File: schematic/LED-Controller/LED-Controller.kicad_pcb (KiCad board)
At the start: 2 copper layers, 40.5 x 36.5 mm, 16 parts, among them J1 5V Power, J10 String6, J2 ICSP, J3 RCin, J4 Serial Connect, J5 String1, J6 String2, J7 String3, J8 String4, J9 String5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

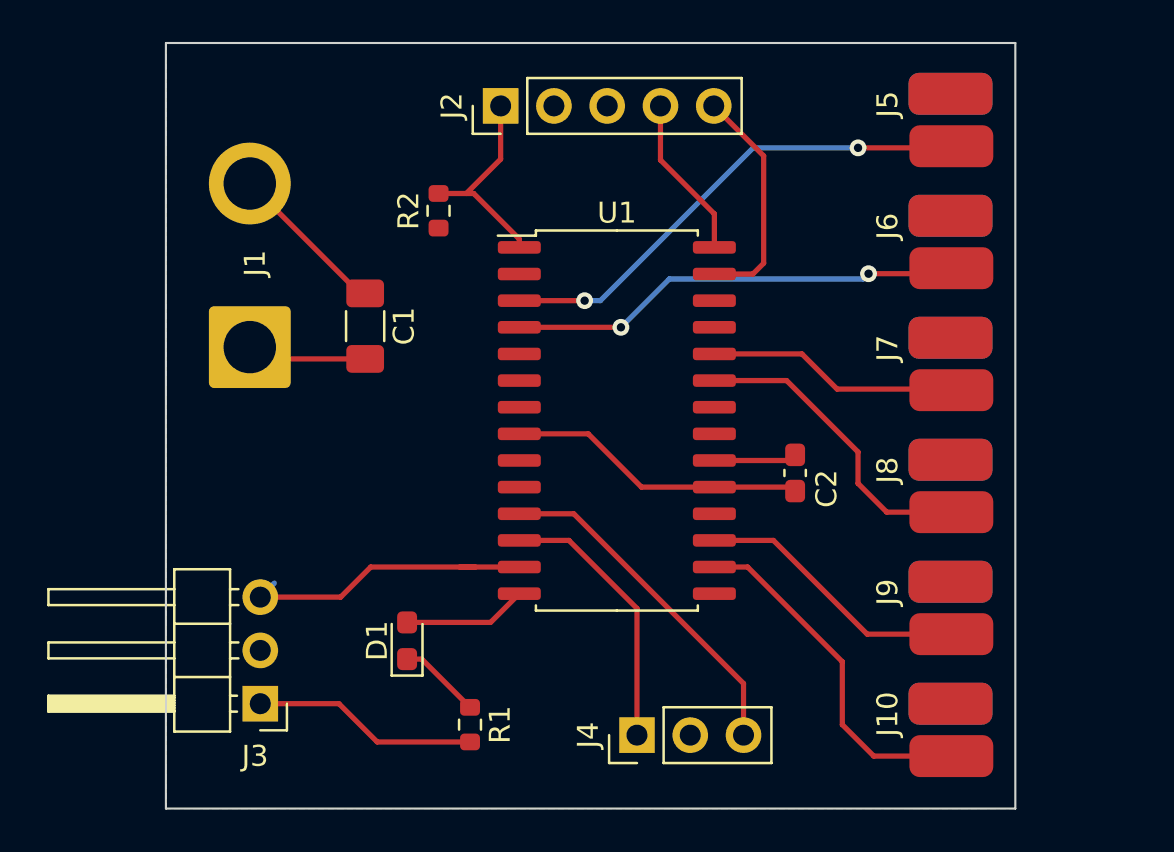
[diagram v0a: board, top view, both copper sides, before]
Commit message: Changed connectors
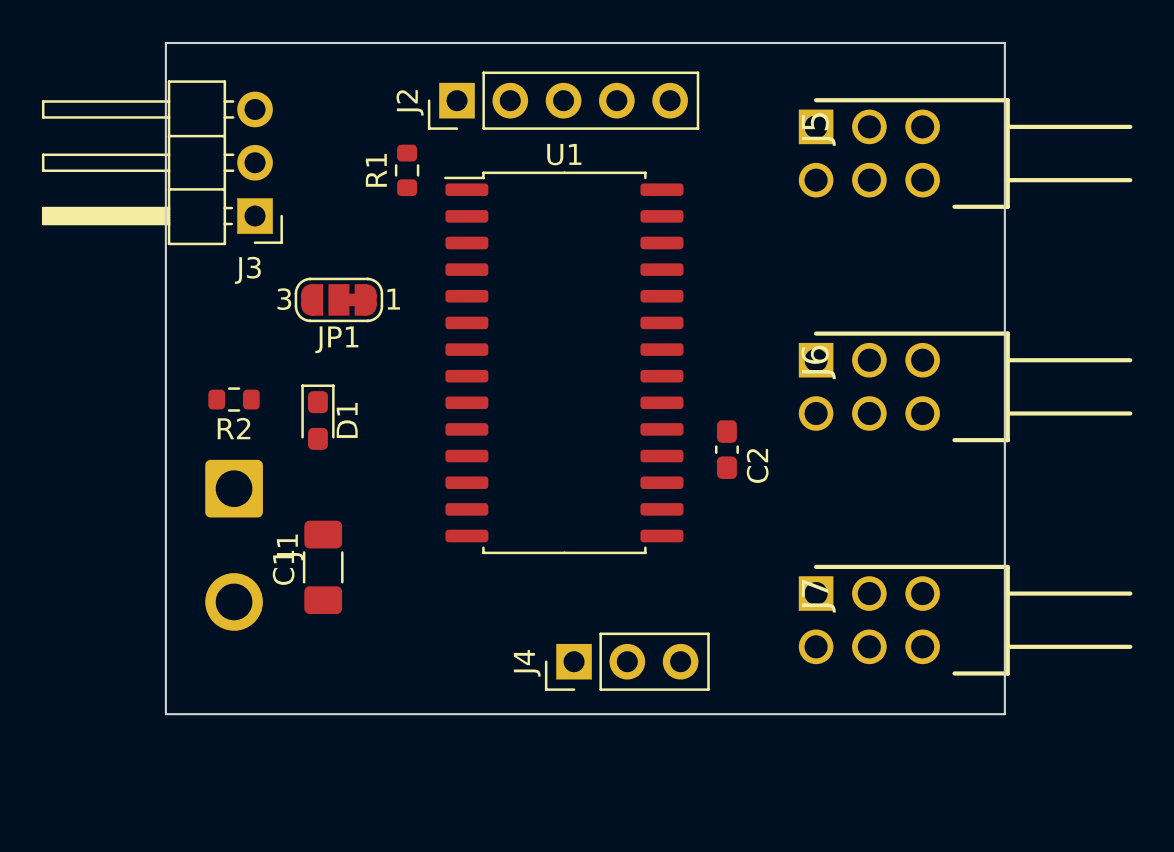
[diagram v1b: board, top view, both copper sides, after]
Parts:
- removed J10: String6, LEDStringConn:TopBottom_3Pin
- removed J8: String4, LEDStringConn:TopBottom_3Pin
- removed J9: String5, LEDStringConn:TopBottom_3Pin
- removed the R1 at (132.5, 102.0)
- added JP1: uC Power, Jumper:SolderJumper-3_P1.3mm_Bridged12_RoundedPad1.0x1.5mm_NumberLabels, F.Cu at (126.2, 81.8)
- added R2: 220, Resistor_SMD:R_0603_1608Metric, F.Cu at (121.2, 86.5)
- J1: footprint Connector_Wire:SolderWire-2sqmm_1x02_P7.8mm_D2mm_OD3.9mm -> Connector_Wire:SolderWire-1sqmm_1x02_P5.4mm_D1.4mm_OD2.7mm
- J5: value String1 -> TSW-102-08-L-T-RA; footprint LEDStringConn:TopBottom_3Pin -> SamacSys_Parts:HDRRA6W64P254_3X2_508X254X810P
- J6: value String2 -> TSW-102-08-L-T-RA; footprint LEDStringConn:TopBottom_3Pin -> SamacSys_Parts:HDRRA6W64P254_3X2_508X254X810P
- J7: value String3 -> TSW-102-08-L-T-RA; footprint LEDStringConn:TopBottom_3Pin -> SamacSys_Parts:HDRRA6W64P254_3X2_508X254X810P
- moved J3 23.3 mm to (122.2, 77.8)
- moved C1 11.7 mm to (125.5, 94.5), turned to 90 degrees
- moved D1 11.3 mm to (125.2, 87.5), turned to 270 degrees
- moved J7 10.5 mm to (149.0, 95.8), turned to 270 degrees
- moved J1 6.79 mm to (121.2, 90.8), turned to 270 degrees
- moved J6 5.88 mm to (149.0, 84.6), turned to 270 degrees
- moved J4 4.61 mm to (137.5, 99.0)
- moved J5 4.02 mm to (149.0, 73.5), turned to 270 degrees
- moved U1 3.72 mm to (137.0, 84.8)
- moved C2 3.44 mm to (144.8, 88.9)
- moved R1 2.44 mm to (129.5, 75.6)
- moved J2 2.09 mm to (131.9, 72.2)
- renumbered R2 to R1
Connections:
- C2 pad 2: VDD -> /uC_Power
- J2 pad 2: VDD -> /uC_Power
- J5 pad 1: VDD -> Net-(J5-Pad1)
- J5 pad 2: Net-(J5-Pad2) -> VDD
- J6 pad 1: VDD -> Net-(J6-Pad1)
- J6 pad 2: Net-(J6-Pad2) -> VDD
- J7 pad 1: VDD -> Net-(J7-Pad1)
- J7 pad 2: Net-(J7-Pad2) -> VDD
- R1 pad 1: VDD -> /uC_Power
- U1 pad 16: Net-(J10-Pad2) -> Net-(J7-Pad4)
- U1 pad 17: Net-(J9-Pad2) -> Net-(J7-Pad1)
- U1 pad 20: VDD -> /uC_Power
- U1 pad 23: Net-(J8-Pad2) -> Net-(J6-Pad4)
- U1 pad 24: Net-(J7-Pad2) -> Net-(J6-Pad1)
- U1 pad 3: Net-(J5-Pad2) -> Net-(J5-Pad1)
- U1 pad 4: Net-(J6-Pad2) -> Net-(J5-Pad4)
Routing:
- net GND: track 31.0 -> 0.00 mm
- net Net-(J5-Pad2): track 23.6 -> 0.00 mm, vias 2 -> 0
- net Net-(J6-Pad2): track 21.8 -> 0.00 mm, vias 2 -> 0
- net Net-(J10-Pad2): track 16.8 -> 0.00 mm
- net Net-(J4-Pad3): track 16.5 -> 0.00 mm
- net Net-(J8-Pad2): track 14.8 -> 0.00 mm
- net Net-(J3-Pad3): track 14.6 -> 0.00 mm
- net Net-(J9-Pad2): track 13.1 -> 0.00 mm
- net Net-(J4-Pad1): track 13.0 -> 0.00 mm
- net Net-(J7-Pad2): track 12.0 -> 0.00 mm
- net VDD: track 11.6 -> 0.00 mm
- net Net-(J2-Pad5): track 11.0 -> 0.00 mm
- net Net-(J2-Pad1): track 10.00 -> 0.00 mm
- net Net-(J2-Pad4): track 7.81 -> 0.00 mm
- net Net-(D1-Pad2): track 5.92 -> 0.00 mm
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- removed copper zone on B.Cu, net GND
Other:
- board size 40.5 x 36.5 mm -> 40 x 32 mm

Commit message: Complete pcb layout
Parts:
- J5, J6, J7: value TSW-102-08-L-T-RA -> (none)
- moved J1 25.5 mm to (146.0, 97.0), turned to 0 degrees
- moved C1 11.7 mm to (137.0, 96.5), turned to 270 degrees
- moved J4 9.54 mm to (128.2, 96.5), turned to 270 degrees
- moved J7 6.75 mm to (148.8, 89.0)
- moved J6 3.38 mm to (148.8, 81.2)
- moved R2 3.09 mm to (122.0, 89.5)
- moved C2 2.65 mm to (145.0, 86.2)
- moved D1 2.46 mm to (126.2, 89.8)
- moved JP1 2.02 mm to (125.2, 83.5)
- moved U1 0.75 mm to (137.0, 84.0)
- moved J2 0.63 mm to (131.5, 71.8)
- moved J5 0.25 mm to (148.8, 73.5)
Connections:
- U1 pad 11: Net-(J4-Pad3) -> Net-(J3-Pad3)
- U1 pad 12: Net-(J4-Pad1) -> Net-(D1-Pad2)
- U1 pad 13: Net-(J3-Pad3) -> Net-(J4-Pad3)
- U1 pad 14: Net-(D1-Pad2) -> Net-(J4-Pad1)
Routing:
- net VDD: track 0.00 -> 81.6 mm, vias 0 -> 2
- net GND: track 0.00 -> 63.5 mm, vias 0 -> 2
- net /uC_Power: track 0.00 -> 38.1 mm, vias 0 -> 3
- net Net-(J3-Pad3): track 0.00 -> 20.3 mm
- net Net-(J5-Pad1): track 0.00 -> 18.4 mm, vias 0 -> 1
- net Net-(J5-Pad4): track 0.00 -> 17.9 mm, vias 0 -> 1
- net Net-(J4-Pad3): track 0.00 -> 12.4 mm
- net Net-(J3-Pad2): track 0.00 -> 9.87 mm
- net Net-(J2-Pad5): track 0.00 -> 9.20 mm
- net Net-(J6-Pad4): track 0.00 -> 7.80 mm
- net Net-(J7-Pad1): track 0.00 -> 7.40 mm
- net Net-(J7-Pad4): track 0.00 -> 7.33 mm
- net Net-(J6-Pad1): track 0.00 -> 7.28 mm
- net Net-(J2-Pad1): track 0.00 -> 7.09 mm
- net Net-(J4-Pad1): track 0.00 -> 7.03 mm
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- added copper zone on B.Cu, net GND
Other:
- board text added: "+"
- board text added: "-"
- board text added: "JLCJLCJLCJLC"
- board text added: "LED Controller"
- board text added: "QES 2021"
- board text added: "V 1.0"

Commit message: Completed pcb
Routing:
- net GND: track 63.5 -> 57.9 mm, vias 2 -> 3
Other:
- rule solder_mask_min_width: 0.25 -> 0.2
- board text added: "1"
- board text added: "2"
- board text added: "3"
- board text added: "4"
- board text added: "5"
- board text added: "6"
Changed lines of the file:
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@@
   (general
     (thickness 1.6)
-    (drawings 42)
-    (tracks 106)
+    (drawings 48)
+    (tracks 108)
     (zones 0)
     (modules 14)
@@
   (page A4)
   (layers
-    (0 F.Cu signal hide)
-    (31 B.Cu signal hide)
+    (0 F.Cu signal)
+    (31 B.Cu signal)
     (32 B.Adhes user hide)
     (33 F.Adhes user hide)
@@
     (36 B.SilkS user)
     (37 F.SilkS user)
-    (38 B.Mask user)
-    (39 F.Mask user)
+    (38 B.Mask user hide)
+    (39 F.Mask user hide)
     (40 Dwgs.User user hide)
     (41 Cmts.User user hide)
@@
     (pad_drill 2.5)
     (pad_to_mask_clearance 0.051)
-    (solder_mask_min_width 0.25)
+    (solder_mask_min_width 0.2)
     (aux_axis_origin 0 0)
     (visible_elements 7FFFFFFF)
@@
     (tags "capacitor handsolder")
     (attr smd)
-    (fp_text reference C2 (at -0.75 1.5 90) (layer F.SilkS)
+    (fp_text reference C2 (at 2.25 -0.5 180) (layer F.SilkS)
       (effects (font (size 1 1) (thickness 0.15)))
     )
@@
       (effects (font (size 0.8 0.8) (thickness 0.12)))
     )
-    (pad 2 smd roundrect (at 1.5625 0 270) (size 1.325 1.8) (layers F.Cu F.Paste F.Mask) (roundrect_rratio 0.1886777358490566)
-      (net 1 GND))
-    (pad 1 smd roundrect (at -1.5625 0 270) (size 1.325 1.8) (layers F.Cu F.Paste F.Mask) (roundrect_rratio 0.1886777358490566)
+    (pad 2 smd roundrect (at 1.5625 0 270) (size 1.325 1.8) (layers F.Cu F.Paste F.Mask) (roundrect_rratio 0.1886769811320755)
+      (net 1 GND))
+    (pad 1 smd roundrect (at -1.5625 0 270) (size 1.325 1.8) (layers F.Cu F.Paste F.Mask) (roundrect_rratio 0.1886769811320755)
       (net 2 VDD))
     (model ${KISYS3DMOD}/Capacitor_SMD.3dshapes/C_1206_3216Metric.wrl
@@
       (rotate (xyz 0 0 0))
     )
+  )
+  (gr_text 6 (at 146.25 91.75) (layer F.SilkS)
+    (effects (font (size 1.6 1.6) (thickness 0.3)))
+  )
+  (gr_text 5 (at 146.25 89.25) (layer F.SilkS)
+    (effects (font (size 1.6 1.6) (thickness 0.3)))
+  )
+  (gr_text 4 (at 146.25 84) (layer F.SilkS)
+    (effects (font (size 1.6 1.6) (thickness 0.3)))
+  )
+  (gr_text 3 (at 146.25 81.5) (layer F.SilkS)
+    (effects (font (size 1.6 1.6) (thickness 0.3)))
+  )
+  (gr_text 2 (at 146.25 76.25) (layer F.SilkS)
+    (effects (font (size 1.6 1.6) (thickness 0.3)))
+  )
+  (gr_text 1 (at 146.25 73.5) (layer F.SilkS)
+    (effects (font (size 1.6 1.6) (thickness 0.3)))
   )
   (gr_line (start 124.5 72.25) (end 125.5 72.25) (layer F.SilkS) (width 0.3))
@@
   (via (at 139.575 87.175) (size 0.8) (drill 0.4) (layers F.Cu B.Cu) (net 1))
   (segment (start 144.9375 98.0625) (end 146 97) (width 0.25) (layer F.Cu) (net 1) (status 30))
-  (segment (start 137 98.0625) (end 144.9375 98.0625) (width 0.25) (layer F.Cu) (net 1) (status 30))
   (segment (start 121.175 89.5) (end 121.175 88.425) (width 0.25) (layer F.Cu) (net 1) (status 10))
   (via (at 121 88.25) (size 0.8) (drill 0.4) (layers F.Cu B.Cu) (net 1))
@@
   (segment (start 146 97) (end 143 97) (width 2) (layer B.Cu) (net 1) (status 40010))
   (segment (start 146 97) (end 148.5 97) (width 2) (layer B.Cu) (net 1) (status 40010))
+  (segment (start 139.1875 98.0625) (end 139.25 98) (width 0.25) (layer F.Cu) (net 1))
+  (via (at 139.25 98) (size 0.8) (drill 0.4) (layers F.Cu B.Cu) (net 1))
+  (segment (start 137 98.0625) (end 139.1875 98.0625) (width 0.25) (layer F.Cu) (net 1))
   (segment (start 137 94.9375) (end 148.0625 94.9375) (width 0.25) (layer F.Cu) (net 2) (status 10))
   (segment (start 150.125 97) (end 151.4 97) (width 0.25) (layer F.Cu) (net 2) (status 30))

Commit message: Moved serial connected to edge of board
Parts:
- moved J4 6.79 mm to (121.5, 97.2), turned to 180 degrees
- moved R2 1.80 mm to (123.0, 88.0)
- moved D1 0.75 mm to (126.2, 89.0)
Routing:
- net Net-(J4-Pad1): track 7.03 -> 12.9 mm
- net GND: track 57.9 -> 52.2 mm
- net Net-(D1-Pad1): track 3.68 -> 2.48 mm
- net Net-(J4-Pad3): track 12.4 -> 11.4 mm
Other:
- board text added: "V 1.1"
- board text removed: "V 1.0"
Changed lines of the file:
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@@
     (thickness 1.6)
     (drawings 48)
-    (tracks 108)
+    (tracks 102)
     (zones 0)
     (modules 14)
@@
   )
   (module Resistor_SMD:R_0603_1608Metric (layer F.Cu)
-    (at 122 89.5 180)
+    (at 123 88 180)
     (descr "Resistor SMD 0603 (1608 Metric), square (rectangular) end terminal, IPC_7351 nominal, (Body size source: IPC-SM-782 page 72, https://www.pcb-3d.com/wordpress/wp-content/uploads/ipc-sm-782a_amendment_1_and_2.pdf), generated with kicad-footprint-generator")
     (tags resistor)
@@
   )
   (module Connector_PinHeader_2.54mm:PinHeader_1x03_P2.54mm_Vertical (layer F.Cu)
-    (at 128.25 96.5 270)
+    (at 121.5 97.25 180)
     (descr "Through hole straight pin header, 1x03, 2.54mm pitch, single row")
     (tags "Through hole pin header THT 1x03 2.54mm single row")
-    (fp_text reference J4 (at 0 -2.33 90) (layer F.SilkS)
-      (effects (font (size 1 1) (thickness 0.15)))
-    )
-    (fp_text value "Serial Connect" (at 0 7.41 90) (layer F.Fab)
+    (fp_text reference J4 (at 0 -2.33) (layer F.SilkS)
+      (effects (font (size 1 1) (thickness 0.15)))
+    )
+    (fp_text value "Serial Connect" (at 0 7.41) (layer F.Fab)
       (effects (font (size 1 1) (thickness 0.15)))
     )
@@
     (fp_line (start 1.27 -1.27) (end 1.27 6.35) (layer F.Fab) (width 0.1))
     (fp_line (start -0.635 -1.27) (end 1.27 -1.27) (layer F.Fab) (width 0.1))
-    (fp_text user %R (at 0 2.54) (layer F.Fab)
-      (effects (font (size 1 1) (thickness 0.15)))
-    )
-    (pad 3 thru_hole oval (at 0 5.08 270) (size 1.7 1.7) (drill 1) (layers *.Cu *.Mask)
+    (fp_text user %R (at 0 2.54 90) (layer F.Fab)
+      (effects (font (size 1 1) (thickness 0.15)))
+    )
+    (pad 3 thru_hole oval (at 0 5.08 180) (size 1.7 1.7) (drill 1) (layers *.Cu *.Mask)
       (net 10 "Net-(J4-Pad3)"))
-    (pad 2 thru_hole oval (at 0 2.54 270) (size 1.7 1.7) (drill 1) (layers *.Cu *.Mask)
-      (net 1 GND))
-    (pad 1 thru_hole rect (at 0 0 270) (size 1.7 1.7) (drill 1) (layers *.Cu *.Mask)
+    (pad 2 thru_hole oval (at 0 2.54 180) (size 1.7 1.7) (drill 1) (layers *.Cu *.Mask)
+      (net 1 GND))
+    (pad 1 thru_hole rect (at 0 0 180) (size 1.7 1.7) (drill 1) (layers *.Cu *.Mask)
       (net 11 "Net-(J4-Pad1)"))
     (model ${KISYS3DMOD}/Connector_PinHeader_2.54mm.3dshapes/PinHeader_1x03_P2.54mm_Vertical.wrl
@@
   )
   (module LED_SMD:LED_0603_1608Metric_Pad1.05x0.95mm_HandSolder (layer F.Cu)
-    (at 126.25 89.75 270)
+    (at 126.25 89 270)
     (descr "LED SMD 0603 (1608 Metric), square (rectangular) end terminal, IPC_7351 nominal, (Body size source: http://www.tortai-tech.com/upload/download/2011102023233369053.pdf), generated with kicad-footprint-generator")
     (tags "LED handsolder")
@@
     (effects (font (size 1.5 1.5) (thickness 0.2)) (justify mirror))
   )
-  (gr_text "V 1.0" (at 142.904762 78) (layer B.SilkS)
+  (gr_text "V 1.1" (at 142.904762 78) (layer B.SilkS)
     (effects (font (size 2 2) (thickness 0.4)) (justify mirror))
   )
@@
   (gr_line (start 118 101.5) (end 118 69.5) (layer Edge.Cuts) (width 0.1))
   (gr_line (start 158 101.5) (end 118 101.5) (layer Edge.Cuts) (width 0.1))
+  (via (at 121 88) (size 0.8) (drill 0.4) (layers F.Cu B.Cu) (net 1))
   (segment (start 144.9375 87.175) (end 145 87.1125) (width 0.25) (layer F.Cu) (net 1) (status 30))
   (segment (start 141.65 87.175) (end 144.9375 87.175) (width 0.25) (layer F.Cu) (net 1) (status 30))
@@
   (via (at 139.575 87.175) (size 0.8) (drill 0.4) (layers F.Cu B.Cu) (net 1))
   (segment (start 144.9375 98.0625) (end 146 97) (width 0.25) (layer F.Cu) (net 1) (status 30))
-  (segment (start 121.175 89.5) (end 121.175 88.425) (width 0.25) (layer F.Cu) (net 1) (status 10))
-  (via (at 121 88.25) (size 0.8) (drill 0.4) (layers F.Cu B.Cu) (net 1))
-  (segment (start 121.175 88.425) (end 121 88.25) (width 0.25) (layer F.Cu) (net 1))
   (segment (start 153.83 91.54) (end 153.83 73.5) (width 2) (layer F.Cu) (net 1) (status 30))
   (segment (start 153.83 83.79) (end 153.83 91.54) (width 2) (layer B.Cu) (net 1) (status 30))
   (segment (start 153.83 81.25) (end 153.83 73.5) (width 2) (layer B.Cu) (net 1) (status 30))
-  (segment (start 146 97) (end 143 97) (width 2) (layer B.Cu) (net 1) (status 40010))
-  (segment (start 146 97) (end 148.5 97) (width 2) (layer B.Cu) (net 1) (status 40010))
   (segment (start 139.1875 98.0625) (end 139.25 98) (width 0.25) (layer F.Cu) (net 1))
   (via (at 139.25 98) (size 0.8) (drill 0.4) (layers F.Cu B.Cu) (net 1))
-  (segment (start 137 98.0625) (end 139.1875 98.0625) (width 0.25) (layer F.Cu) (net 1))
+  (segment (start 137 98.0625) (end 139.1875 98.0625) (width 0.25) (layer F.Cu) (net 1) (status 10))
+  (segment (start 122.175 88) (end 121 88) (width 0.25) (layer F.Cu) (net 1))
   (segment (start 137 94.9375) (end 148.0625 94.9375) (width 0.25) (layer F.Cu) (net 2) (status 10))
   (segment (start 150.125 97) (end 151.4 97) (width 0.25) (layer F.Cu) (net 2) (status 30))
@@
   (segment (start 127 83.95) (end 126.55 83.5) (width 0.25) (layer F.Cu) (net 2) (status 30))
   (segment (start 127 86.25) (end 127 83.95) (width 0.25) (layer F.Cu) (net 2) (status 20))
-  (segment (start 126.25 90.625) (end 128.375 90.625) (width 0.25) (layer F.Cu) (net 3) (status 10))
-  (segment (start 129.285 89.715) (end 132.35 89.715) (width 0.25) (layer F.Cu) (net 3) (status 20))
-  (segment (start 128.375 90.625) (end 129.285 89.715) (width 0.25) (layer F.Cu) (net 3))
-  (segment (start 122.825 89.5) (end 124 89.5) (width 0.25) (layer F.Cu) (net 4) (status 10))
-  (segment (start 124.625 88.875) (end 126.25 88.875) (width 0.25) (layer F.Cu) (net 4) (status 20))
-  (segment (start 124 89.5) (end 124.625 88.875) (width 0.25) (layer F.Cu) (net 4))
+  (segment (start 126.41 89.715) (end 126.25 89.875) (width 0.25) (layer F.Cu) (net 3))
+  (segment (start 132.35 89.715) (end 126.41 89.715) (width 0.25) (layer F.Cu) (net 3))
+  (segment (start 126.125 88) (end 126.25 88.125) (width 0.25) (layer F.Cu) (net 4))
+  (segment (start 123.825 88) (end 126.125 88) (width 0.25) (layer F.Cu) (net 4))
   (segment (start 141.66 71.75) (end 144.75 74.84) (width 0.25) (layer F.Cu) (net 5) (status 10))
   (segment (start 144.75 74.84) (end 144.75 76.25) (width 0.25) (layer F.Cu) (net 5))
@@
   (segment (start 123.95 81.8) (end 123.95 83.5) (width 0.25) (layer F.Cu) (net 9) (status 20))
   (segment (start 124.5 81.25) (end 123.95 81.8) (width 0.25) (layer F.Cu) (net 9))
-  (segment (start 123.17 96.5) (end 123.17 94.83) (width 0.25) (layer F.Cu) (net 10) (status 10))
-  (segment (start 123.17 94.83) (end 125 93) (width 0.25) (layer F.Cu) (net 10))
-  (segment (start 125 93) (end 128.25 93) (width 0.25) (layer F.Cu) (net 10))
-  (segment (start 130.265 90.985) (end 132.35 90.985) (width 0.25) (layer F.Cu) (net 10) (status 20))
-  (segment (start 128.25 93) (end 130.265 90.985) (width 0.25) (layer F.Cu) (net 10))
-  (segment (start 128.25 96.5) (end 128.25 94.5) (width 0.25) (layer F.Cu) (net 11) (status 10))
-  (segment (start 130.495 92.255) (end 132.35 92.255) (width 0.25) (layer F.Cu) (net 11) (status 20))
-  (segment (start 128.25 94.5) (end 130.495 92.255) (width 0.25) (layer F.Cu) (net 11))
+  (segment (start 132.35 90.985) (end 131.015 90.985) (width 0.25) (layer F.Cu) (net 10) (status 10))
+  (segment (start 131.015 90.985) (end 129.75 92.25) (width 0.25) (layer F.Cu) (net 10))
+  (segment (start 121.58 92.25) (end 121.5 92.17) (width 0.25) (layer F.Cu) (net 10) (status 30))
+  (segment (start 129.75 92.25) (end 121.58 92.25) (width 0.25) (layer F.Cu) (net 10) (status 20))
+  (segment (start 130.745 92.255) (end 125.75 97.25) (width 0.25) (layer F.Cu) (net 11))
+  (segment (start 132.35 92.255) (end 130.745 92.255) (width 0.25) (layer F.Cu) (net 11) (status 10))
+  (segment (start 125.75 97.25) (end 121.5 97.25) (width 0.25) (layer F.Cu) (net 11) (status 20))
   (segment (start 141.65 85.905) (end 143.345 85.905) (width 0.25) (layer F.Cu) (net 24) (status 10))
   (segment (start 143.8625 85.3875) (end 145 85.3875) (width 0.25) (layer F.Cu) (net 24) (status 20))
